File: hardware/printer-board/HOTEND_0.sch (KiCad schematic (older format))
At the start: 7 parts, among them J2 HOT_END, Q2 WSK220N04

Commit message: update,
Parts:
- J2: footprint footprint-lib:s2b-ph-kl,hotend_output -> footprint-lib:mpt_0,5%2f2-2,54
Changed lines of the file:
@@
 $Descr A4 11693 8268
 encoding utf-8
-Sheet 27 34
+Sheet 27 33
 Title ""
 Date ""
@@
 F 0 "J2" H 5219 2825 50  0000 C CNN
 F 1 "HOT_END" H 5219 2916 50  0000 C CNN
-F 2 "footprint-lib:s2b-ph-kl,hotend_output" H 5300 3150 50  0001 C CNN
+F 2 "footprint-lib:mpt_0,5%2f2-2,54" H 5300 3150 50  0001 C CNN
 F 3 "~" H 5300 3150 50  0001 C CNN
 	1    5300 3150

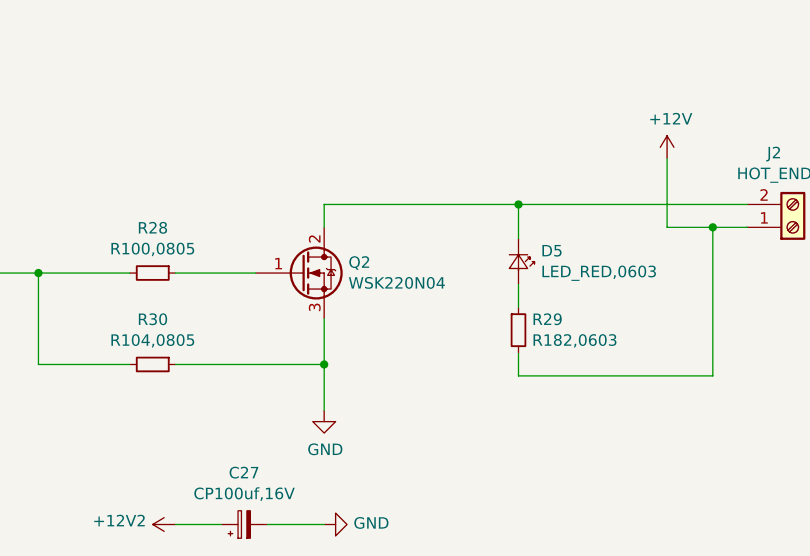
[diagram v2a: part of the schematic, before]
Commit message: update hotend MOSFET,
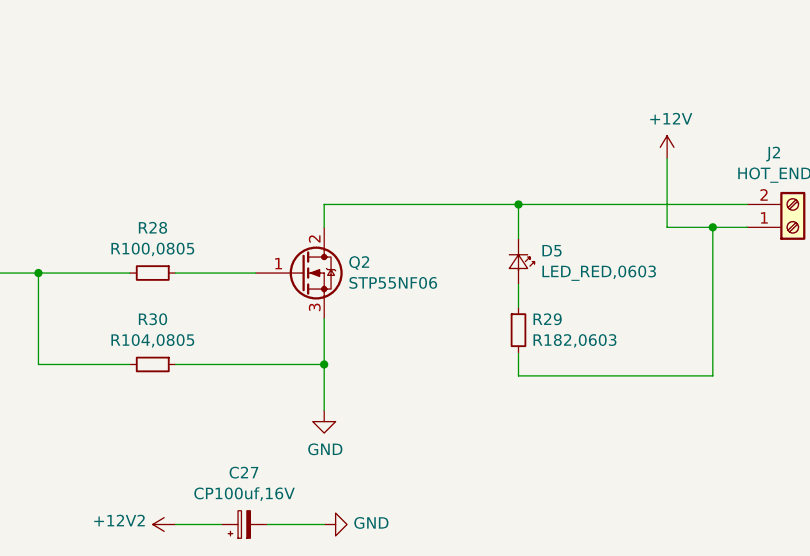
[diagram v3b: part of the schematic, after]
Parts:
- Q2: value WSK220N04 -> STP55NF06
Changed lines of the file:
@@
 AR Path="/5CC22025/5CC222D0/5CC22325" Ref="Q2"  Part="1"
 F 0 "Q2" H 3356 3396 50  0000 L CNN
-F 1 "WSK220N04" H 3356 3305 50  0000 L CNN
+F 1 "STP55NF06" H 3356 3305 50  0000 L CNN
 F 2 "Package_TO_SOT_SMD:TO-263-2" H 3350 3450 50  0001 C CNN
 F 3 "~" H 3150 3350 50  0001 C CNN

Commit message: update,
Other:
- moved on the sheet: D5, J2, R29
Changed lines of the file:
@@
 L Connector:Screw_Terminal_01x02 J?
 U 1 1 5CC19EB5
-P 5300 3150
+P 5300 2950
 AR Path="/5CC0B758/5CC19EB5" Ref="J?"  Part="1"
 AR Path="/5CC12903/5CC19EB5" Ref="J?"  Part="1"
 AR Path="/5CC130A8/5CC19EB5" Ref="J?"  Part="1"
 AR Path="/5CC22025/5CC222D0/5CC19EB5" Ref="J2"  Part="1"
-F 0 "J2" H 5219 2825 50  0000 C CNN
-F 1 "HOT_END" H 5219 2916 50  0000 C CNN
-F 2 "footprint-lib:mpt_0,5%2f2-2,54" H 5300 3150 50  0001 C CNN
-F 3 "~" H 5300 3150 50  0001 C CNN
-	1    5300 3150
-	1    0    0    1
+F 0 "J2" H 5219 2625 50  0000 C CNN
+F 1 "HOT_END" H 5219 2716 50  0000 C CNN
+F 2 "footprint-lib:mpt_0,5%2f2-2,54" H 5300 2950 50  0001 C CNN
+F 3 "~" H 5300 2950 50  0001 C CNN
+	1    5300 2950
+	1    0    0    -1
 $EndComp
 $Comp
@@
 L taobao-r:R182,0603 R?
 U 1 1 5CC2239E
-P 4100 3600
+P 4100 2500
 AR Path="/5CC0B758/5CC2239E" Ref="R?"  Part="1"
 AR Path="/5CC12903/5CC2239E" Ref="R?"  Part="1"
 AR Path="/5CC130A8/5CC2239E" Ref="R?"  Part="1"
 AR Path="/5CC22025/5CC222D0/5CC2239E" Ref="R29"  Part="1"
-F 0 "R29" H 4159 3646 50  0000 L CNN
-F 1 "R182,0603" H 4159 3555 50  0000 L CNN
-F 2 "Resistor_SMD:R_0603_1608Metric_Pad1.05x0.95mm_HandSolder" H 4100 3600 50  0001 C CNN
-F 3 "~" H 4100 3600 50  0001 C CNN
-	1    4100 3600
-	1    0    0    -1
+F 0 "R29" H 4159 2546 50  0000 L CNN
+F 1 "R182,0603" H 4159 2455 50  0000 L CNN
+F 2 "Resistor_SMD:R_0603_1608Metric_Pad1.05x0.95mm_HandSolder" H 4100 2500 50  0001 C CNN
+F 3 "~" H 4100 2500 50  0001 C CNN
+	1    4100 2500
+	1    0    0    1
 $EndComp
 $Comp
 L taobao-led:LED_RED,0603 D?
 U 1 1 5CC2232A
-P 4100 3300
+P 4100 2800
 AR Path="/5CC0B758/5CC2232A" Ref="D?"  Part="1"
 AR Path="/5CC12903/5CC2232A" Ref="D?"  Part="1"
 AR Path="/5CC130A8/5CC2232A" Ref="D?"  Part="1"
 AR Path="/5CC22025/5CC222D0/5CC2232A" Ref="D5"  Part="1"
-F 0 "D5" V 4054 3398 50  0000 L CNN
-F 1 "LED_RED,0603" V 4145 3398 50  0000 L CNN
-F 2 "LED_SMD:LED_0603_1608Metric_Pad1.05x0.95mm_HandSolder" V 4100 3300 50  0001 C CNN
-F 3 "" V 4100 3300 50  0001 C CNN
-	1    4100 3300
-	0    1    1    0
+F 0 "D5" V 4054 2898 50  0000 L CNN
+F 1 "LED_RED,0603" V 4145 2898 50  0000 L CNN
+F 2 "LED_SMD:LED_0603_1608Metric_Pad1.05x0.95mm_HandSolder" V 4100 2800 50  0001 C CNN
+F 3 "" V 4100 2800 50  0001 C CNN
+	1    4100 2800
+	0    1    -1   0
 $EndComp
 Wire Wire Line
@@
 	3250 3050 3250 3150
 Wire Wire Line
-	4100 3200 4100 3050
+	4100 2900 4100 3050
 Connection ~ 4100 3050
 Wire Wire Line
 	4100 3050 3250 3050
 Wire Wire Line
-	4100 3400 4100 3500
+	4100 2700 4100 2600
 Wire Wire Line
-	5100 3150 4950 3150
+	5100 2950 4950 2950
 Wire Wire Line
-	4950 3150 4950 3800
+	4950 2950 4950 2300
 Wire Wire Line
-	4950 3800 4100 3800
+	4950 2300 4800 2300
 Wire Wire Line
-	4100 3800 4100 3700
-Connection ~ 4950 3150
+	4100 2300 4100 2400
 Text HLabel 1500 900  0    50   Input ~ 0
 HOTEND_EN
@@
 L power:+12V #PWR0233
 U 1 1 5CC223A3
-P 4750 2850
-F 0 "#PWR0233" H 4750 2700 50  0001 C CNN
-F 1 "+12V" H 4765 3023 50  0000 C CNN
-F 2 "" H 4750 2850 50  0001 C CNN
-F 3 "" H 4750 2850 50  0001 C CNN
-	1    4750 2850
-	1    0    0    -1
+P 4800 2000
+F 0 "#PWR0233" H 4800 1850 50  0001 C CNN
+F 1 "+12V" H 4815 2173 50  0000 C CNN
+F 2 "" H 4800 2000 50  0001 C CNN
+F 3 "" H 4800 2000 50  0001 C CNN
+	1    4800 2000
+	-1   0    0    -1
 $EndComp
 Wire Wire Line
-	4750 2850 4750 3150
+	4800 2000 4800 2300
+Connection ~ 4800 2300
 Wire Wire Line
-	4750 3150 4950 3150
+	4800 2300 4100 2300
 $EndSCHEMATC

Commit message: update,
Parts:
- removed C27: CP100uf,16V, Capacitor_SMD:CP_Elec_6.3x5.3, symbol taobao-cp:CP100uf,16V
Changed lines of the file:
@@
 $Descr A4 11693 8268
 encoding utf-8
-Sheet 25 32
+Sheet 23 32
 Title ""
 Date ""
@@
 Wire Wire Line
 	2000 3350 2400 3350
-$Comp
-L taobao-components:+12V2 #PWR?
-U 1 1 5CC223A0
-P 2600 4450
-AR Path="/5CC0B758/5CC223A0" Ref="#PWR?"  Part="1"
-AR Path="/5CC12903/5CC223A0" Ref="#PWR?"  Part="1"
-AR Path="/5CC130A8/5CC223A0" Ref="#PWR?"  Part="1"
-AR Path="/5CC22025/5CC222D0/5CC223A0" Ref="#PWR0231"  Part="1"
-F 0 "#PWR0231" H 2600 4300 50  0001 C CNN
-F 1 "+12V2" V 2615 4578 50  0000 L CNN
-F 2 "" H 2600 4450 50  0001 C CNN
-F 3 "" H 2600 4450 50  0001 C CNN
-	1    2600 4450
-	0    -1   -1   0
-$EndComp
-$Comp
-L power:GND #PWR?
-U 1 1 5CC2232C
-P 3250 4450
-AR Path="/5CC0B758/5CC2232C" Ref="#PWR?"  Part="1"
-AR Path="/5CC12903/5CC2232C" Ref="#PWR?"  Part="1"
-AR Path="/5CC130A8/5CC2232C" Ref="#PWR?"  Part="1"
-AR Path="/5CC22025/5CC222D0/5CC2232C" Ref="#PWR0232"  Part="1"
-F 0 "#PWR0232" H 3250 4200 50  0001 C CNN
-F 1 "GND" V 3255 4322 50  0000 R CNN
-F 2 "" H 3250 4450 50  0001 C CNN
-F 3 "" H 3250 4450 50  0001 C CNN
-	1    3250 4450
-	0    -1   -1   0
-$EndComp
-$Comp
-L taobao-cp:CP100uf,16V C27
-U 1 1 5CC223A2
-P 2900 4450
-F 0 "C27" V 3125 4450 50  0000 C CNN
-F 1 "CP100uf,16V" V 3034 4450 50  0000 C CNN
-F 2 "Capacitor_SMD:CP_Elec_6.3x5.3" H 2900 4450 50  0001 C CNN
-F 3 "~" H 2900 4450 50  0001 C CNN
-	1    2900 4450
-	0    -1   -1   0
-$EndComp
-Wire Wire Line
-	2600 4450 2800 4450
-Wire Wire Line
-	3000 4450 3250 4450
 $Bitmap
 Pos 9550 5000

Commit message: update,
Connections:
- net HOTEND_EN renamed EN1
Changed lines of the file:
@@
 	4100 2300 4100 2400
 Text HLabel 1500 900  0    50   Input ~ 0
-HOTEND_EN
+EN1
 Text Label 2300 900  2    50   ~ 0
-HOTEND_EN
+EN1
 Wire Wire Line
 	1500 900  2300 900
 Text Label 1350 3350 0    50   ~ 0
-HOTEND_EN
+EN1
 Wire Wire Line
 	1350 3350 2000 3350

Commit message: update heater layouts,
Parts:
- J2: footprint footprint-lib:mpt_0,5%2f2-2,54 -> footprint-lib:mpt_0,5%2f2-2,54,hotend
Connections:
- net -12V: now reaches D5.1 (K), J2.2 (Pin_2), Q2.2 (D)
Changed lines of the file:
@@
 EESchema Schematic File Version 4
-LIBS:printer-board-cache
+LIBS:HOTEND_0-cache
 EELAYER 26 0
 EELAYER END
 $Descr A4 11693 8268
 encoding utf-8
-Sheet 23 32
+Sheet 1 1
 Title ""
 Date ""
@@
 AR Path="/5CC130A8/5CC19EB5" Ref="J?"  Part="1"
 AR Path="/5CC22025/5CC222D0/5CC19EB5" Ref="J2"  Part="1"
-F 0 "J2" H 5219 2625 50  0000 C CNN
-F 1 "HOT_END" H 5219 2716 50  0000 C CNN
-F 2 "footprint-lib:mpt_0,5%2f2-2,54" H 5300 2950 50  0001 C CNN
+AR Path="/5CC19EB5" Ref="J2"  Part="1"
+F 0 "J2" H 5400 2950 50  0000 L CNN
+F 1 "HOT_END" H 5400 2850 50  0000 L CNN
+F 2 "footprint-lib:mpt_0,5%2f2-2,54,hotend" H 5300 2950 50  0001 C CNN
 F 3 "~" H 5300 2950 50  0001 C CNN
 	1    5300 2950
@@
 AR Path="/5CC130A8/5CC22325" Ref="Q?"  Part="1"
 AR Path="/5CC22025/5CC222D0/5CC22325" Ref="Q2"  Part="1"
+AR Path="/5CC22325" Ref="Q2"  Part="1"
 F 0 "Q2" H 3356 3396 50  0000 L CNN
 F 1 "STP55NF06" H 3356 3305 50  0000 L CNN
@@
 AR Path="/5CC130A8/5CC19EC3" Ref="R?"  Part="1"
 AR Path="/5CC22025/5CC222D0/5CC19EC3" Ref="R28"  Part="1"
+AR Path="/5CC19EC3" Ref="R28"  Part="1"
 F 0 "R28" V 2304 3350 50  0000 C CNN
 F 1 "R100,0805" V 2395 3350 50  0000 C CNN
@@
 AR Path="/5CC130A8/5CC22411" Ref="R?"  Part="1"
 AR Path="/5CC22025/5CC222D0/5CC22411" Ref="R30"  Part="1"
+AR Path="/5CC22411" Ref="R30"  Part="1"
 F 0 "R30" V 2304 3750 50  0000 C CNN
 F 1 "R104,0805" V 2395 3750 50  0000 C CNN
@@
 AR Path="/5CC130A8/5CC22328" Ref="#PWR?"  Part="1"
 AR Path="/5CC22025/5CC222D0/5CC22328" Ref="#PWR0230"  Part="1"
+AR Path="/5CC22328" Ref="#PWR0230"  Part="1"
 F 0 "#PWR0230" H 3250 3700 50  0001 C CNN
 F 1 "GND" H 3255 3777 50  0000 C CNN
@@
 AR Path="/5CC130A8/5CC2239E" Ref="R?"  Part="1"
 AR Path="/5CC22025/5CC222D0/5CC2239E" Ref="R29"  Part="1"
+AR Path="/5CC2239E" Ref="R29"  Part="1"
 F 0 "R29" H 4159 2546 50  0000 L CNN
 F 1 "R182,0603" H 4159 2455 50  0000 L CNN
@@
 AR Path="/5CC130A8/5CC2232A" Ref="D?"  Part="1"
 AR Path="/5CC22025/5CC222D0/5CC2232A" Ref="D5"  Part="1"
+AR Path="/5CC2232A" Ref="D5"  Part="1"
 F 0 "D5" V 4054 2898 50  0000 L CNN
 F 1 "LED_RED,0603" V 4145 2898 50  0000 L CNN
@@
 Wire Wire Line
 	4800 2300 4100 2300
+Text Label 4800 3050 2    50   ~ 0
+-12V
+Text Label 4550 2300 2    50   ~ 0
+12V_led
 $EndSCHEMATC
